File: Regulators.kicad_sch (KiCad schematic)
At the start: 22 parts, among them J5 24V Logic, J6 24V Peripheral, U2 XL1509-12, U3 XL1509-5.0

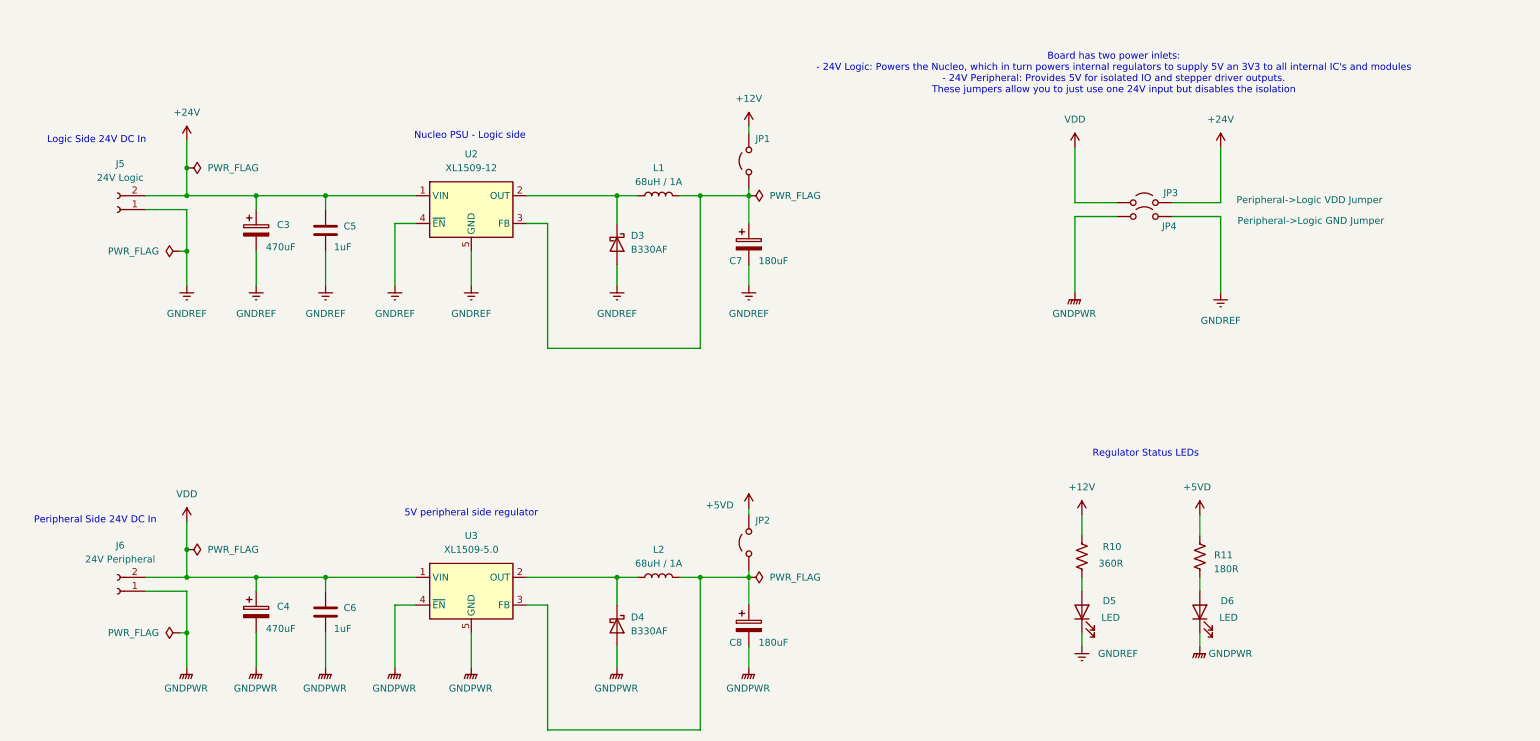
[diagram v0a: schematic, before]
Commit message: Changes to input after testing with some optical sensors
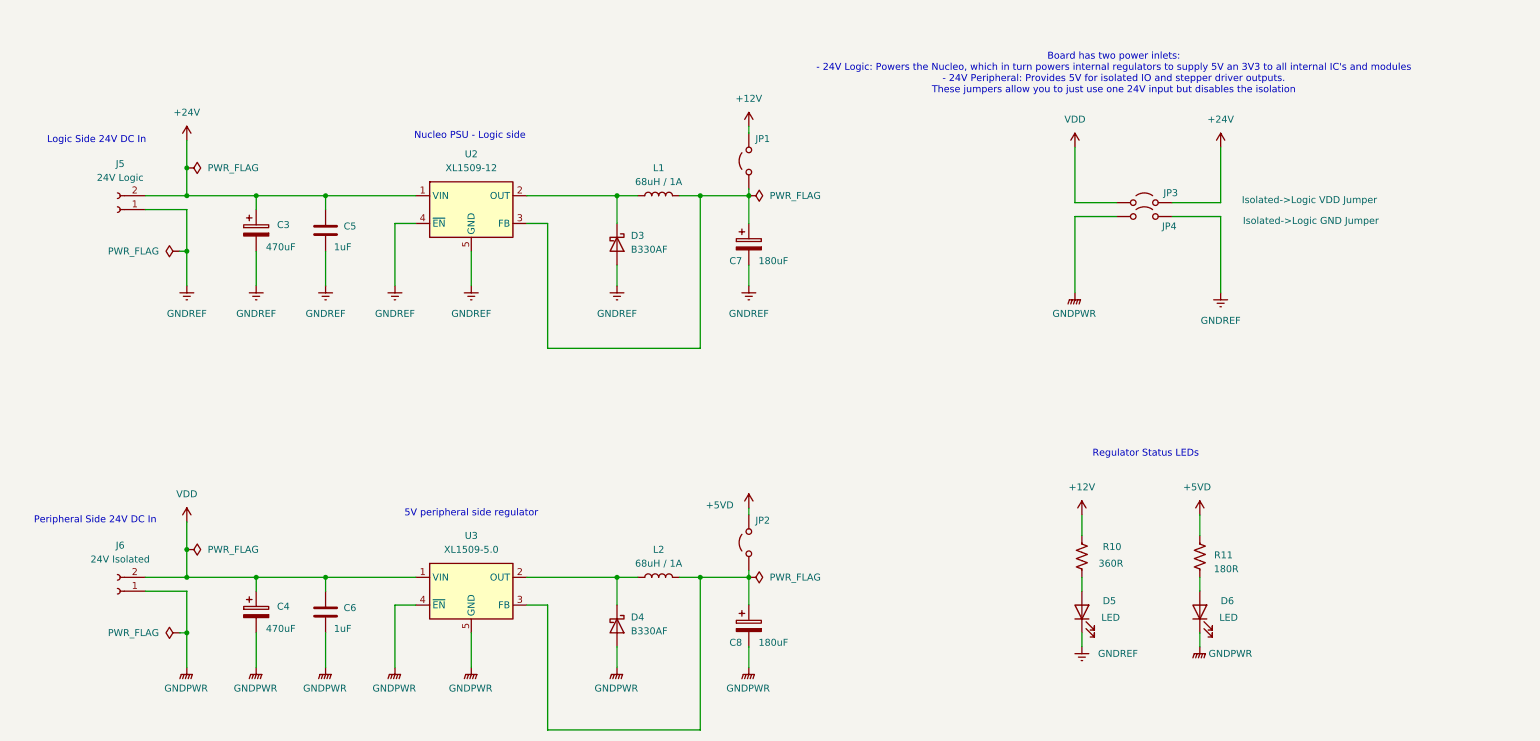
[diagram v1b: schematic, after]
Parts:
- J6: value 24V Peripheral -> 24V Isolated
- JP3: value Peripheral->Logic VDD Jumper -> Isolated->Logic VDD Jumper
- JP4: value Peripheral->Logic GND Jumper -> Isolated->Logic GND Jumper
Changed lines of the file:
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@@
 			)
 		)
-		(property "Value" "Peripheral->Logic GND Jumper"
+		(property "Value" "Isolated->Logic GND Jumper"
 			(at 256.54 55.372 0)
 			(effects
@@
 			)
 		)
-		(property "Value" "Peripheral->Logic VDD Jumper"
+		(property "Value" "Isolated->Logic VDD Jumper"
 			(at 256.286 51.562 0)
 			(effects
@@
 			)
 		)
-		(property "Value" "24V Peripheral"
+		(property "Value" "24V Isolated"
 			(at 38.608 117.348 0)
 			(effects

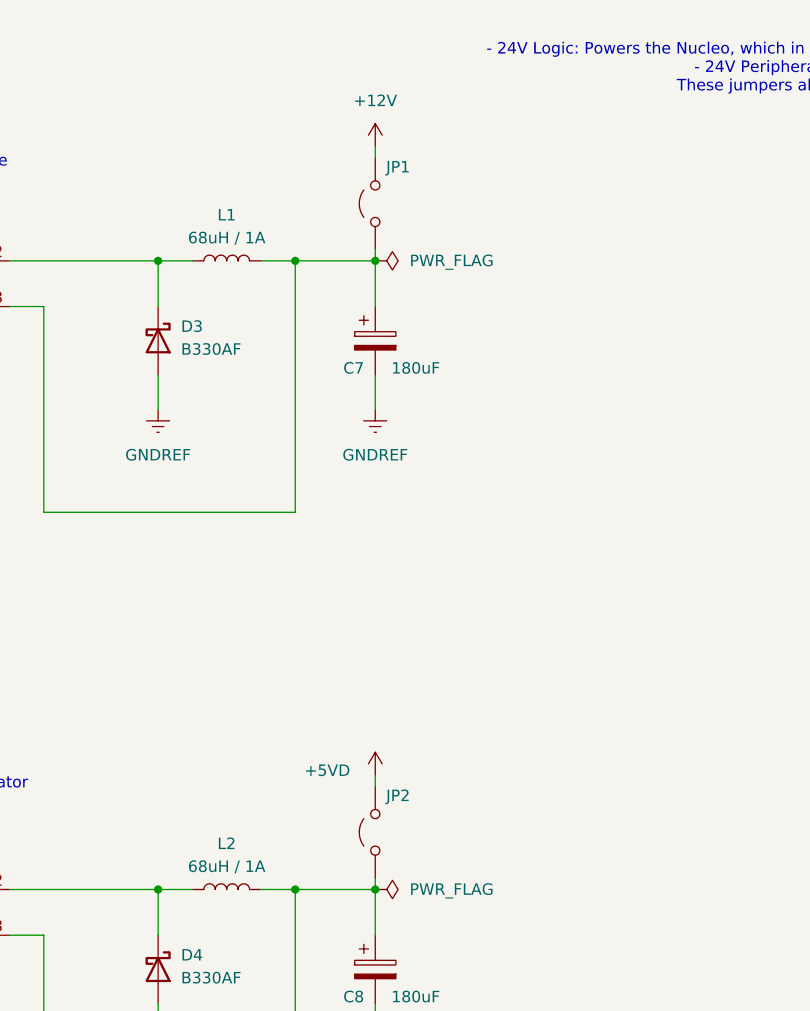
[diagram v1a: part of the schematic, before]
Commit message: Added Analog inputs, updates to readme re powering board from external supply
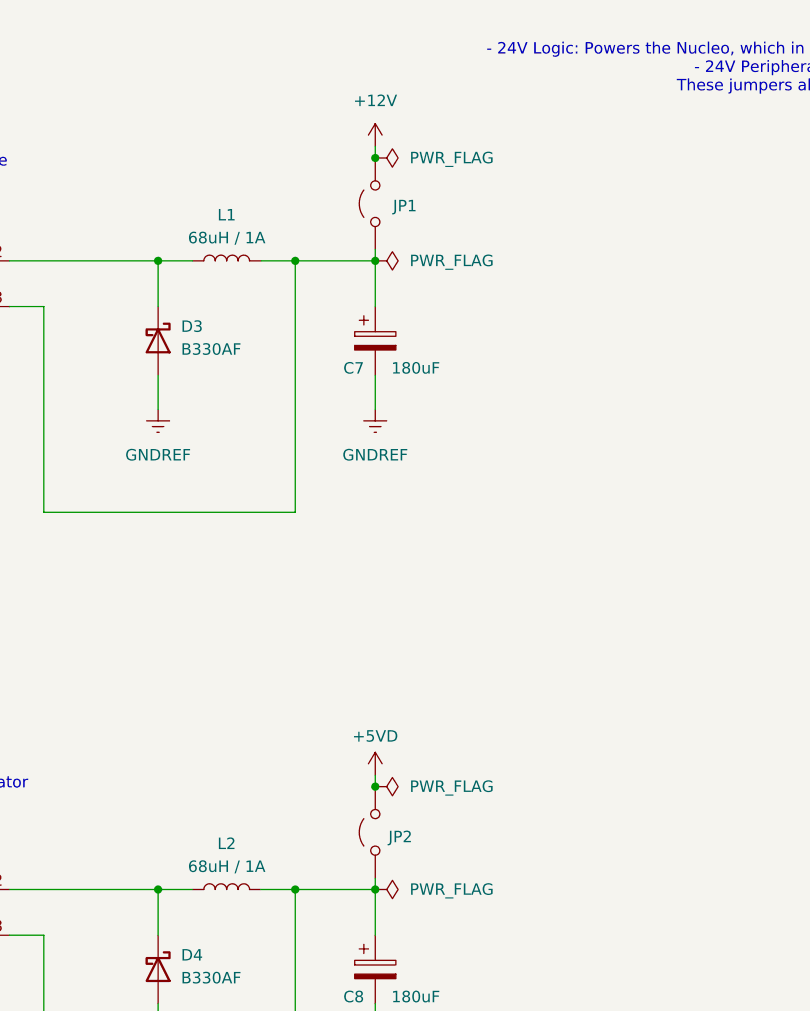
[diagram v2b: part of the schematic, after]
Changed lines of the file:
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@@
 	)
 	(junction
+		(at 153.67 39.37)
+		(diameter 0)
+		(color 0 0 0 0)
+	)
+	(junction
 		(at 63.5 120.65)
 		(diameter 0)
@@
 	)
 	(junction
+		(at 153.67 109.22)
+		(diameter 0)
+		(color 0 0 0 0)
+	)
+	(junction
 		(at 76.2 120.65)
 		(diameter 0)
@@
 		)
 		(property "Value" "+5VD"
-			(at 148.336 107.442 0)
+			(at 153.67 103.632 0)
 			(effects
 				(font
@@
 	)
 	(symbol
+		(lib_id "power:PWR_FLAG")
+		(at 153.67 109.22 270)
+		(unit 1)
+		(exclude_from_sim no)
+		(in_bom yes)
+		(on_board no)
+		(dnp no)
+		(property "Reference" "#FLG09"
+			(at 155.575 109.22 0)
+			(effects
+				(font
+					(size 1.27 1.27)
+				)
+				(hide yes)
+			)
+		)
+		(property "Value" "PWR_FLAG"
+			(at 157.48 109.22 90)
+			(effects
+				(font
+					(size 1.27 1.27)
+				)
+				(justify left)
+			)
+		)
+		(property "Footprint" ""
+			(at 153.67 109.22 0)
+			(effects
+				(font
+					(size 1.27 1.27)
+				)
+				(hide yes)
+			)
+		)
+		(property "Datasheet" "~"
+			(at 153.67 109.22 0)
+			(effects
+				(font
+					(size 1.27 1.27)
+				)
+				(hide yes)
+			)
+		)
+		(property "Description" "Special symbol for telling ERC where power comes from"
+			(at 153.67 109.22 0)
+			(effects
+				(font
+					(size 1.27 1.27)
+				)
+				(hide yes)
+			)
+		)
+		(pin "1"
+		)
+		(instances
+			(project "Remora Nucleo F446ZE Hat"
+				(path "/5473abc6-7b93-43cc-a401-f691c4d7d7cf/e0dc83df-f7d9-4488-bd0b-6c0af36f8703"
+					(reference "#FLG09")
+					(unit 1)
+				)
+			)
+		)
+	)
+	(symbol
 		(lib_id "Device:C_Polarized")
 		(at 153.67 59.69 0)
@@
 		(dnp no)
 		(fields_autoplaced yes)
-		(property "Reference" "#FLG06"
+		(property "Reference" "#FLG05"
 			(at 52.705 45.72 0)
 			(effects
@@
 			(project "Remora Nucleo F446RE Hat"
 				(path "/5473abc6-7b93-43cc-a401-f691c4d7d7cf/e0dc83df-f7d9-4488-bd0b-6c0af36f8703"
-					(reference "#FLG06")
+					(reference "#FLG05")
 					(unit 1)
 				)
@@
 		(dnp no)
 		(fields_autoplaced yes)
-		(property "Reference" "#FLG04"
+		(property "Reference" "#FLG03"
 			(at 47.625 60.96 0)
 			(effects
@@
 			(project "Remora Nucleo F446ZE Hat"
 				(path "/5473abc6-7b93-43cc-a401-f691c4d7d7cf/e0dc83df-f7d9-4488-bd0b-6c0af36f8703"
-					(reference "#FLG04")
+					(reference "#FLG03")
 					(unit 1)
 				)
@@
 	)
 	(symbol
+		(lib_id "power:PWR_FLAG")
+		(at 153.67 39.37 270)
+		(unit 1)
+		(exclude_from_sim no)
+		(in_bom yes)
+		(on_board no)
+		(dnp no)
+		(property "Reference" "#FLG07"
+			(at 155.575 39.37 0)
+			(effects
+				(font
+					(size 1.27 1.27)
+				)
+				(hide yes)
+			)
+		)
+		(property "Value" "PWR_FLAG"
+			(at 157.48 39.37 90)
+			(effects
+				(font
+					(size 1.27 1.27)
+				)
+				(justify left)
+			)
+		)
+		(property "Footprint" ""
+			(at 153.67 39.37 0)
+			(effects
+				(font
+					(size 1.27 1.27)
+				)
+				(hide yes)
+			)
+		)
+		(property "Datasheet" "~"
+			(at 153.67 39.37 0)
+			(effects
+				(font
+					(size 1.27 1.27)
+				)
+				(hide yes)
+			)
+		)
+		(property "Description" "Special symbol for telling ERC where power comes from"
+			(at 153.67 39.37 0)
+			(effects
+				(font
+					(size 1.27 1.27)
+				)
+				(hide yes)
+			)
+		)
+		(pin "1"
+		)
+		(instances
+			(project "Remora Nucleo F446ZE Hat"
+				(path "/5473abc6-7b93-43cc-a401-f691c4d7d7cf/e0dc83df-f7d9-4488-bd0b-6c0af36f8703"
+					(reference "#FLG07")
+					(unit 1)
+				)
+			)
+		)
+	)
+	(symbol
 		(lib_id "Device:L")
 		(at 137.16 50.8 90)
@@
 		(dnp no)
 		(property "Reference" "JP2"
-			(at 156.21 110.236 90)
+			(at 156.464 114.808 90)
 			(effects
 				(font
@@
 		(dnp no)
 		(fields_autoplaced yes)
-		(property "Reference" "#FLG07"
+		(property "Reference" "#FLG06"
 			(at 52.705 115.57 0)
 			(effects
@@
 			(project "Remora Nucleo F446ZE Hat"
 				(path "/5473abc6-7b93-43cc-a401-f691c4d7d7cf/e0dc83df-f7d9-4488-bd0b-6c0af36f8703"
-					(reference "#FLG07")
+					(reference "#FLG06")
 					(unit 1)
 				)
@@
 		(dnp no)
 		(fields_autoplaced yes)
-		(property "Reference" "#FLG05"
+		(property "Reference" "#FLG04"
 			(at 47.625 130.81 0)
 			(effects
@@
 			(project "Remora Nucleo F446ZE Hat"
 				(path "/5473abc6-7b93-43cc-a401-f691c4d7d7cf/e0dc83df-f7d9-4488-bd0b-6c0af36f8703"
-					(reference "#FLG05")
+					(reference "#FLG04")
 					(unit 1)
 				)
@@
 		(dnp no)
 		(property "Reference" "JP1"
-			(at 156.21 40.386 90)
+			(at 156.972 44.704 90)
 			(effects
 				(font
@@
 		(dnp no)
 		(fields_autoplaced yes)
-		(property "Reference" "#FLG09"
+		(property "Reference" "#FLG010"
 			(at 155.575 120.65 0)
 			(effects
@@
 			(project "Remora Nucleo F446RE Hat"
 				(path "/5473abc6-7b93-43cc-a401-f691c4d7d7cf/e0dc83df-f7d9-4488-bd0b-6c0af36f8703"
-					(reference "#FLG09")
+					(reference "#FLG010")
 					(unit 1)
 				)

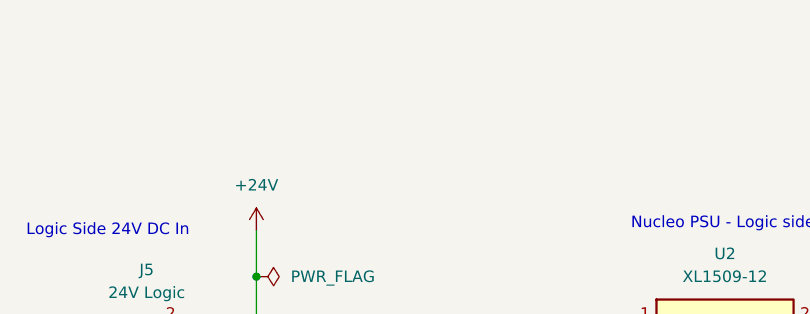
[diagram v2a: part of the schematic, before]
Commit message: Finalised Spindle DAC, working as expected
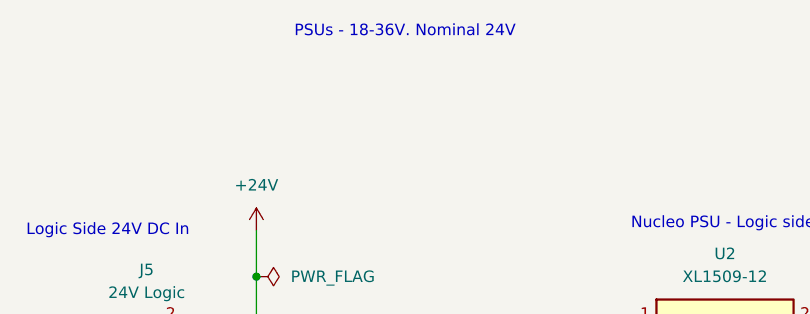
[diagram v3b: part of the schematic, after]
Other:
- note added: "PSUs - 18-36V. Nominal 24V"
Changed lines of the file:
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@@
+		)
+	)
+	(text "PSUs - 18-36V. Nominal 24V"
+		(exclude_from_sim no)
+		(at 67.31 18.542 0)
+		(effects
+			(font
+				(size 1.27 1.27)
+			)
 		)
 	)

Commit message: Added high speed encoder input circuitry. General tidy and updates to readme
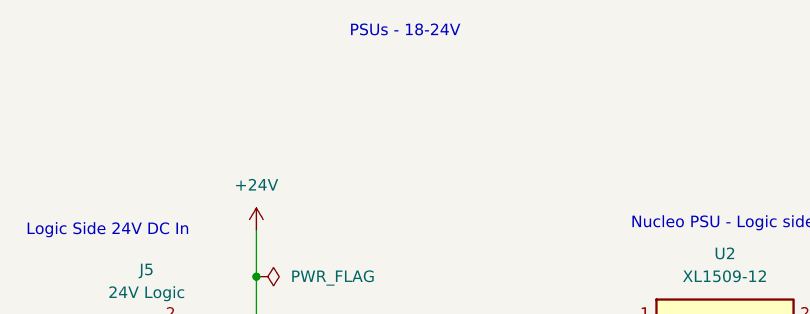
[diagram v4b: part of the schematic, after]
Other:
- note added: "PSUs - 18-24V"
- note removed: "PSUs - 18-36V. Nominal 24V"
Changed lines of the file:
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@@
 		)
 	)
-	(text "PSUs - 18-36V. Nominal 24V"
+	(text "PSUs - 18-24V"
 		(exclude_from_sim no)
 		(at 67.31 18.542 0)

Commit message: Switched terminal footprints over to a finer pitch. Corrected an issue with component reference values preventing proper use of multi channel rule areas. Component references for 4 channel optos are more straightforward as a result
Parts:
- J5, J6: footprint EBWA_02_A:ADAMTECH_EBWA-02-A -> 691412120002B:691412120002B; Digikey Part Number 1818-QT02ADP83V0000G-ND -> 732-691412120002B-ND; Digikey URL https://www.digikey.com.au/en/products/detail/amphenol-anyt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 -> https://www.digikey.com.au/en/products/detail/w%C3%BCrth-el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
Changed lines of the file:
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@@
 			)
 		)
-		(property "Footprint" "EBWA_02_A:ADAMTECH_EBWA-02-A"
+		(property "Footprint" "691412120002B:691412120002B"
 			(at 38.1 53.34 0)
 			(effects
@@
 			)
 		)
-		(property "Digikey Part Number" "1818-QT02ADP83V0000G-ND"
+		(property "Digikey Part Number" "732-691412120002B-ND"
 			(at 38.1 53.34 0)
 			(effects
@@
 			)
 		)
-		(property "Digikey URL" "https://www.digikey.com.au/en/products/detail/amphenol-anytek/QT02ADP83V0000G/25618889"
+		(property "Digikey URL" "https://www.digikey.com.au/en/products/detail/w%C3%BCrth-elektronik/691412120002B/11478592"
 			(at 38.1 53.34 0)
 			(effects
@@
 			)
 		)
-		(property "Footprint" "EBWA_02_A:ADAMTECH_EBWA-02-A"
+		(property "Footprint" "691412120002B:691412120002B"
 			(at 38.1 123.19 0)
 			(effects
@@
 			)
 		)
-		(property "Digikey Part Number" "1818-QT02ADP83V0000G-ND"
+		(property "Digikey Part Number" "732-691412120002B-ND"
 			(at 38.1 123.19 0)
 			(effects
@@
 			)
 		)
-		(property "Digikey URL" "https://www.digikey.com.au/en/products/detail/amphenol-anytek/QT02ADP83V0000G/25618889"
+		(property "Digikey URL" "https://www.digikey.com.au/en/products/detail/w%C3%BCrth-elektronik/691412120002B/11478592"
 			(at 38.1 123.19 0)
 			(effects
